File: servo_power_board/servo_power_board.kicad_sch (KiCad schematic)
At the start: 16 parts, among them J1 Conn_01x02_Pin, J2 Conn_01x02_Socket, J3 Conn_01x02_Socket, J4 Conn_01x02_Socket, J5 Conn_01x02_Socket, U1 YDS512F

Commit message: サーボ電源基板　コンデンサを入手性により変更
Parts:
- C1: value 220u -> 330u; footprint Capacitor_THT:CP_Radial_D10.0mm_P5.00mm -> PCM_Capacitor_THT_AKL:CP_Radial_D10.0mm_P5.00mm_H23mm_Horizontal1; Buy_URL https://akizukidenshi.com/catalog/g/g102718/ -> https://akizukidenshi.com/catalog/g/g117499/
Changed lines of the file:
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@@
 			)
 		)
-		(property "Value" "220u"
+		(property "Value" "330u"
 			(at 48.006 53.34 90)
 			(show_name no)
@@
 			)
 		)
-		(property "Footprint" "Capacitor_THT:CP_Radial_D10.0mm_P5.00mm"
+		(property "Footprint" "PCM_Capacitor_THT_AKL:CP_Radial_D10.0mm_P5.00mm_H23mm_Horizontal1"
 			(at 50.4952 48.26 0)
 			(hide yes)
@@
 			)
 		)
-		(property "Description" "220μF35V"
+		(property "Description" "330μF63V"
 			(at 49.53 44.45 0)
 			(hide yes)
@@
 			)
 		)
-		(property "Buy_URL" "https://akizukidenshi.com/catalog/g/g102718/"
+		(property "Buy_URL" "https://akizukidenshi.com/catalog/g/g117499/"
 			(at 49.53 44.45 90)
 			(hide yes)

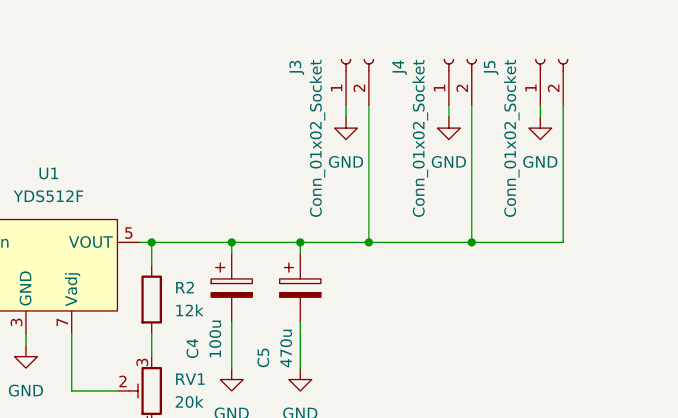
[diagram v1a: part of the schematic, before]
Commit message: サーボ電源基板　電圧モニタ用コネクタを追加
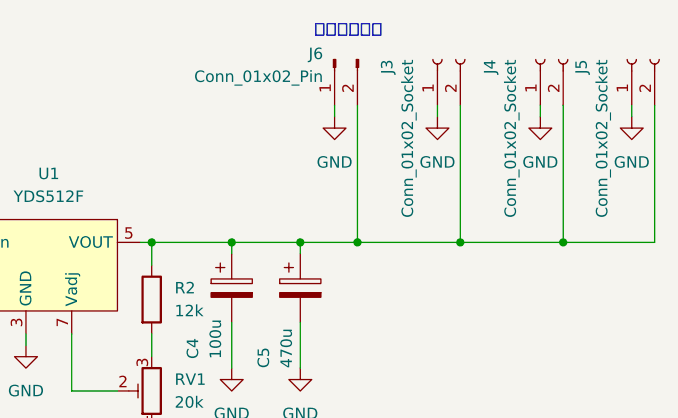
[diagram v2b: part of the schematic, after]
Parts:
- added J6: Conn_01x02_Pin, OU_connector:DF1EC-2P-2.5DSA, symbol Connector:Conn_01x02_Pin
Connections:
- net GND: now also J6.1 (Pin_1)
- net at C4.1, C5.1, J3.2 (Pin_2)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: now also J6.2 (Pin_2)
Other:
- note added: "電圧モニタ用"
- moved on the sheet: J3, J4, J5

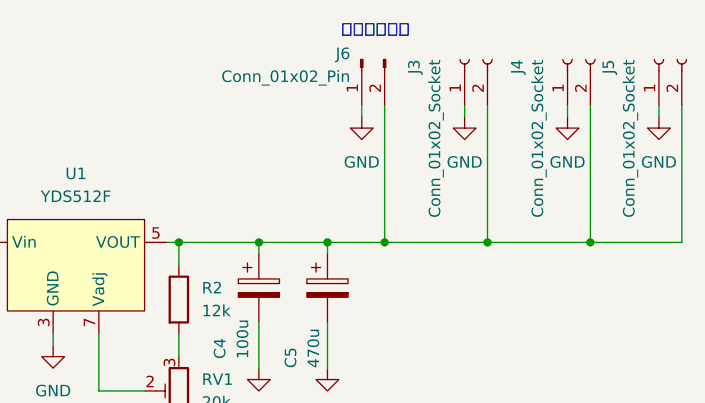
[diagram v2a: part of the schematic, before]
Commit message: サーボ電源基板　アノテーションを更新
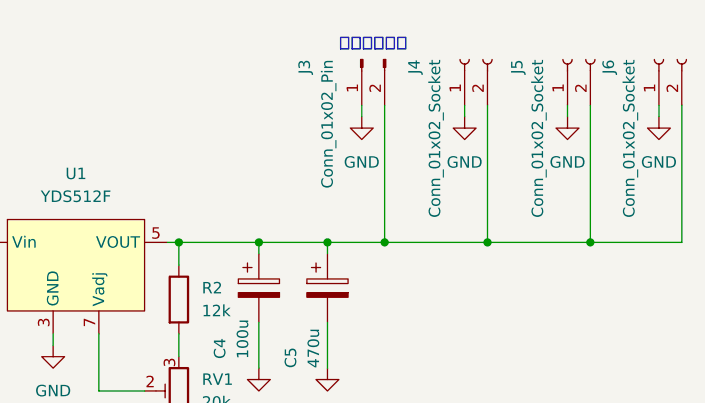
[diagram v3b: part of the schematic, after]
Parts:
- renumbered J6 to J3, J3 to J4, J4 to J5, J5 to J6
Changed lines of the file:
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@@
 	(text "電圧モニタ用"
 		(exclude_from_sim no)
-		(at 109.474 16.002 0)
+		(at 109.22 17.526 0)
 		(effects
 			(font
@@
 		(dnp no)
 		(fields_autoplaced yes)
-		(property "Reference" "#PWR013"
+		(property "Reference" "#PWR014"
 			(at 140.97 31.75 0)
 			(hide yes)
@@
 			(project "servo_power_board"
 				(path "/715b1808-9db1-495e-bdf5-a7d74f3e3bb8"
-					(reference "#PWR013")
+					(reference "#PWR014")
 					(unit 1)
 				)
@@
 		(in_pos_files yes)
 		(dnp no)
-		(property "Reference" "J3"
+		(property "Reference" "J4"
 			(at 113.792 19.05 0)
 			(show_name no)
@@
 			(project "servo_power_board"
 				(path "/715b1808-9db1-495e-bdf5-a7d74f3e3bb8"
-					(reference "J3")
+					(reference "J4")
 					(unit 1)
 				)
@@
 		(in_pos_files yes)
 		(dnp no)
-		(property "Reference" "J5"
+		(property "Reference" "J6"
 			(at 135.382 19.05 0)
 			(show_name no)
@@
 			(project "servo_power_board"
 				(path "/715b1808-9db1-495e-bdf5-a7d74f3e3bb8"
-					(reference "J5")
+					(reference "J6")
 					(unit 1)
 				)
@@
 		(in_pos_files yes)
 		(dnp no)
-		(property "Reference" "J4"
+		(property "Reference" "J5"
 			(at 125.222 19.05 0)
 			(show_name no)
@@
 			(project "servo_power_board"
 				(path "/715b1808-9db1-495e-bdf5-a7d74f3e3bb8"
-					(reference "J4")
+					(reference "J5")
 					(unit 1)
 				)
@@
 		(dnp no)
 		(fields_autoplaced yes)
-		(property "Reference" "#PWR012"
+		(property "Reference" "#PWR013"
 			(at 130.81 31.75 0)
 			(hide yes)
@@
 			(project "servo_power_board"
 				(path "/715b1808-9db1-495e-bdf5-a7d74f3e3bb8"
-					(reference "#PWR012")
+					(reference "#PWR013")
 					(unit 1)
 				)
@@
 		(dnp no)
 		(fields_autoplaced yes)
-		(property "Reference" "#PWR014"
+		(property "Reference" "#PWR011"
 			(at 107.95 31.75 0)
 			(hide yes)
@@
 			(project "servo_power_board"
 				(path "/715b1808-9db1-495e-bdf5-a7d74f3e3bb8"
-					(reference "#PWR014")
+					(reference "#PWR011")
 					(unit 1)
 				)
@@
 		(dnp no)
 		(fields_autoplaced yes)
-		(property "Reference" "#PWR011"
+		(property "Reference" "#PWR012"
 			(at 119.38 31.75 0)
 			(hide yes)
@@
 			(project "servo_power_board"
 				(path "/715b1808-9db1-495e-bdf5-a7d74f3e3bb8"
-					(reference "#PWR011")
+					(reference "#PWR012")
 					(unit 1)
 				)
@@
 		(in_pos_files yes)
 		(dnp no)
-		(property "Reference" "J6"
-			(at 106.68 18.4149 90)
+		(property "Reference" "J3"
+			(at 101.6 19.05 0)
 			(show_name no)
 			(do_not_autoplace no)
@@
 		)
 		(property "Value" "Conn_01x02_Pin"
-			(at 106.68 20.9549 90)
+			(at 104.14 19.05 0)
 			(show_name no)
 			(do_not_autoplace no)
@@
 			(project "servo_power_board"
 				(path "/715b1808-9db1-495e-bdf5-a7d74f3e3bb8"
-					(reference "J6")
+					(reference "J3")
 					(unit 1)
 				)

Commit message: サーボ電源基板　基板にテストポイントを追加，ver 0.2
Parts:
- added TP1: TestPoint, TestPoint:TestPoint_THTPad_D2.0mm_Drill1.0mm, symbol Connector:TestPoint
- added TP2: TestPoint_Probe, TestPoint:TestPoint_THTPad_D2.0mm_Drill1.0mm, symbol Connector:TestPoint_Probe
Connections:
- net GND: now also TP1.1
- net at C4.1, C5.1, J3.2 (Pin_2)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: now also TP2.1
